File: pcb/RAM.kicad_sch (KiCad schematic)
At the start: 29 parts, among them U2 MT41K64M16TW-x

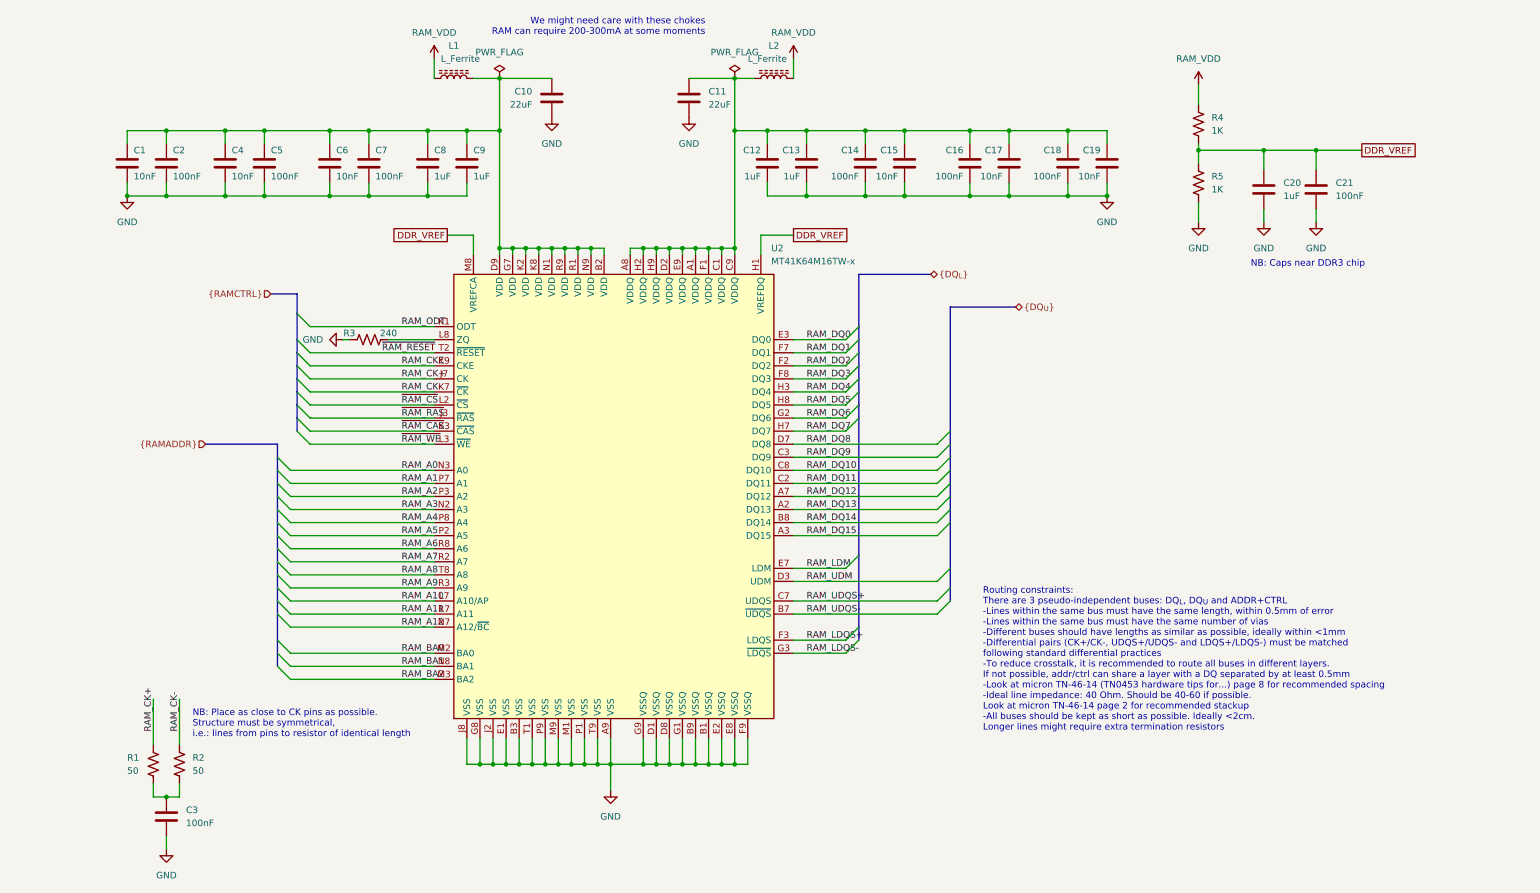
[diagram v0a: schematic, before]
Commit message: Initial footprint assignment
- Some edits to the schematic to improve readability
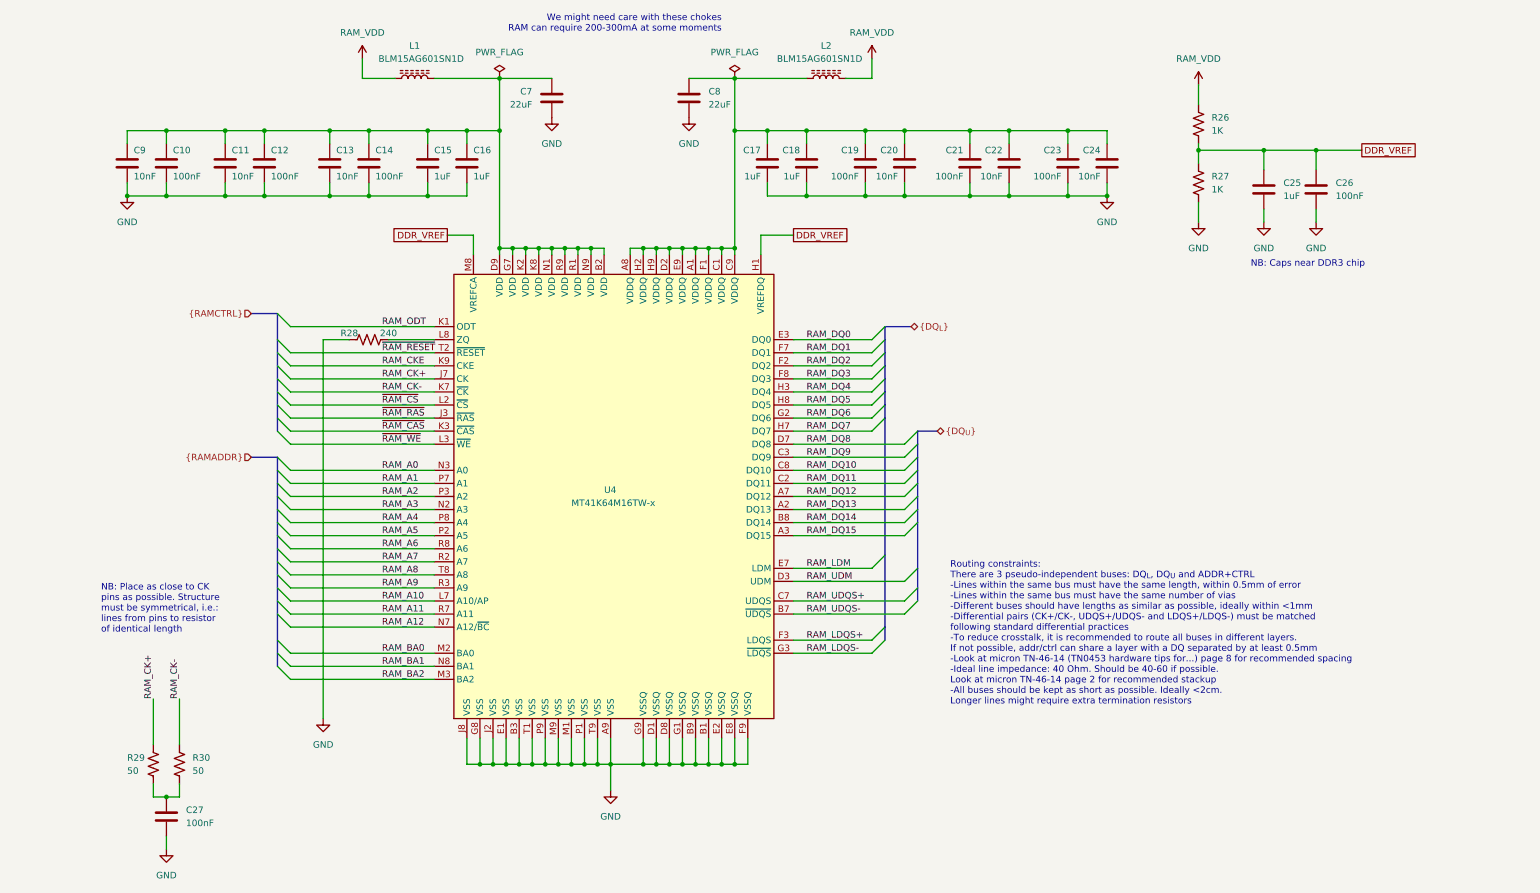
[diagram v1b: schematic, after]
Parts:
- C10: renamed from C2; footprint (none) -> Capacitor_SMD:C_0402_1005Metric
- C11: renamed from C4; footprint (none) -> Capacitor_SMD:C_0402_1005Metric
- C12: renamed from C5; footprint (none) -> Capacitor_SMD:C_0402_1005Metric
- C13: renamed from C6; footprint (none) -> Capacitor_SMD:C_0402_1005Metric
- C14: renamed from C7; footprint (none) -> Capacitor_SMD:C_0402_1005Metric
- C15: renamed from C8; footprint (none) -> Capacitor_SMD:C_0805_2012Metric
- C16: renamed from C9; footprint (none) -> Capacitor_SMD:C_0805_2012Metric
- C17: renamed from C12; footprint (none) -> Capacitor_SMD:C_0805_2012Metric
- C18: renamed from C13; footprint (none) -> Capacitor_SMD:C_0805_2012Metric
- C19: renamed from C14; footprint (none) -> Capacitor_SMD:C_0402_1005Metric
- C20: renamed from C15; footprint (none) -> Capacitor_SMD:C_0402_1005Metric
- C21: renamed from C16; footprint (none) -> Capacitor_SMD:C_0402_1005Metric
- C22: renamed from C17; footprint (none) -> Capacitor_SMD:C_0402_1005Metric
- C23: renamed from C18; footprint (none) -> Capacitor_SMD:C_0402_1005Metric
- C24: renamed from C19; footprint (none) -> Capacitor_SMD:C_0402_1005Metric
- C25: renamed from C20; footprint (none) -> Capacitor_SMD:C_0805_2012Metric
- C26: renamed from C21; footprint (none) -> Capacitor_SMD:C_0402_1005Metric
- C27: renamed from C3; footprint (none) -> Capacitor_SMD:C_0402_1005Metric
- C7: renamed from C10; footprint (none) -> Capacitor_SMD:C_1210_3225Metric
- C8: renamed from C11; footprint (none) -> Capacitor_SMD:C_1210_3225Metric
- C9: renamed from C1; footprint (none) -> Capacitor_SMD:C_0402_1005Metric
- L1, L2: value L_Ferrite -> BLM15AG601SN1D; footprint (none) -> Inductor_SMD:L_0402_1005Metric
- R26: renamed from R4; footprint (none) -> Resistor_SMD:R_0402_1005Metric
- R27: renamed from R5; footprint (none) -> Resistor_SMD:R_0402_1005Metric
- R28: renamed from R3; footprint (none) -> Resistor_SMD:R_0402_1005Metric
- R29: renamed from R1; footprint (none) -> Resistor_SMD:R_0402_1005Metric
- R30: renamed from R2; footprint (none) -> Resistor_SMD:R_0402_1005Metric
- U4: renamed from U2; footprint Package_BGA:BGA-96_9.0x13.0mm_Layout2x3x16_P0.8mm -> jonnew:MICRON_BGA96-10.5x8x1.3
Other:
- company: OEPS -> OEPS & Open Ephys, Inc.
- title: ECP5U85-BSE-USB Breakout board -> ECP5U85-BSE-USB Breakout Board
- moved on the sheet: L1, L2

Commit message: Rough PCB component placement
- This will change
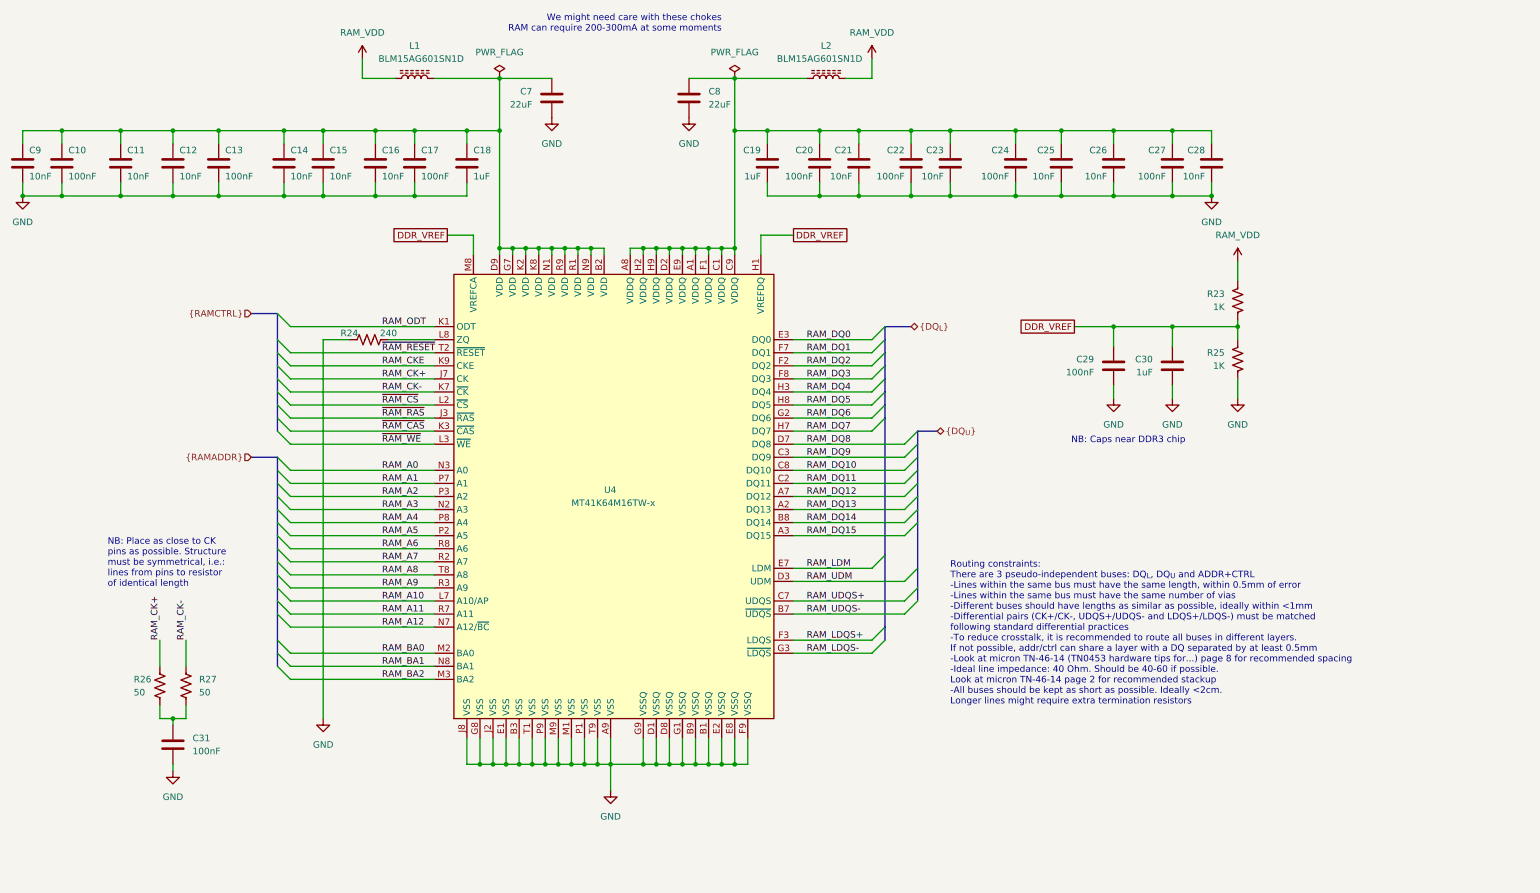
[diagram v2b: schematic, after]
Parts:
- removed C14: 100nF, Capacitor_SMD:C_0402_1005Metric, symbol Device:C
- removed C18: 1uF, Capacitor_SMD:C_0805_2012Metric, symbol Device:C
- added C12, C16, C25, C26, C28: 10nF, Capacitor_SMD:C_0402_1005Metric, symbol Device:C
- added C27: 100nF, Capacitor_SMD:C_0402_1005Metric, symbol Device:C
- C15: value 1uF -> 10nF; footprint Capacitor_SMD:C_0805_2012Metric -> Capacitor_SMD:C_0402_1005Metric
- C17: value 1uF -> 100nF; footprint Capacitor_SMD:C_0805_2012Metric -> Capacitor_SMD:C_0402_1005Metric
- C18: renamed from C16; footprint Capacitor_SMD:C_0805_2012Metric -> Capacitor_SMD:C_0603_1608Metric
- C19: value 100nF -> 1uF; footprint Capacitor_SMD:C_0402_1005Metric -> Capacitor_SMD:C_0603_1608Metric
- C20, C22, C24: value 10nF -> 100nF
- C21, C23: value 100nF -> 10nF
- C30: renamed from C25; footprint Capacitor_SMD:C_0805_2012Metric -> Capacitor_SMD:C_0603_1608Metric
- renumbered C12 to C13, C13 to C14, C26 to C29, C27 to C31, R26 to R23, R28 to R24, R27 to R25, R29 to R26, R30 to R27
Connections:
- net GND: now also C12.2, C16.2, C25.2, C26.2, C27.2, C28.2
- net at C10.1, C11.1, C13.1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: now also C17.1, C12.1, C16.1
- net at C19.1, C20.1, C21.1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: now also C25.1, C26.1, C27.1, C28.1; no longer C17.1
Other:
- moved on the sheet: C10, C11, C13, C14, C29, C30, C31, C9, R23, R25, R26, R27

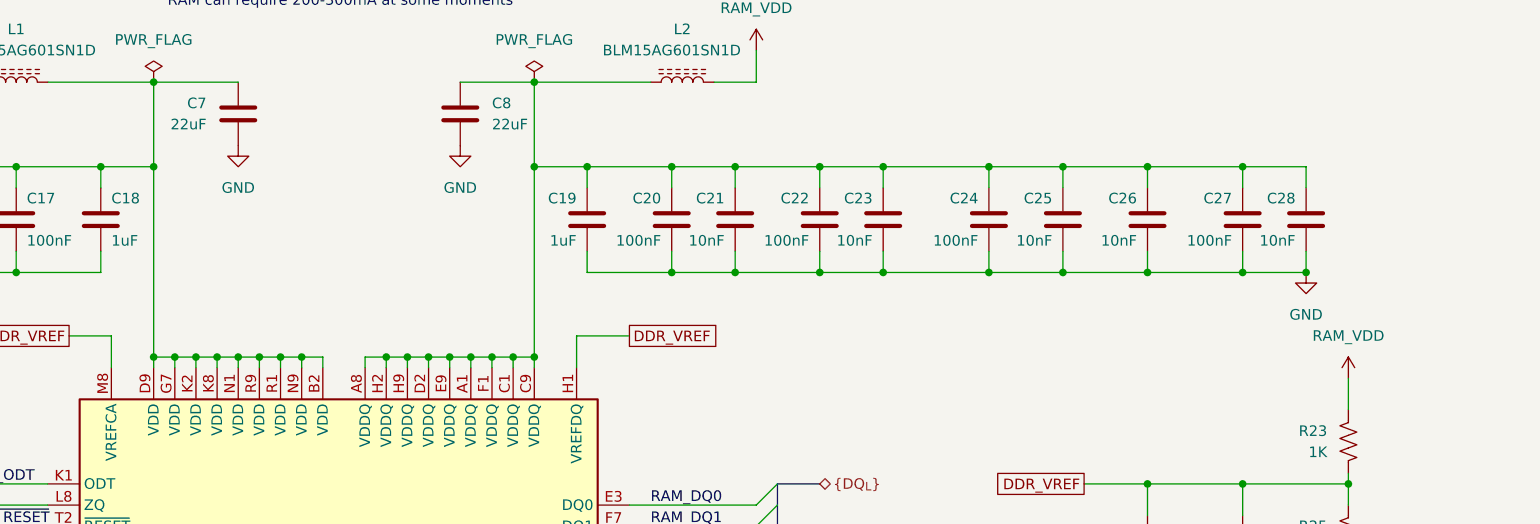
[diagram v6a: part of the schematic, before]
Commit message: Most of power routing
- Will need to retune the lengths again as final step, but only after
power is complete
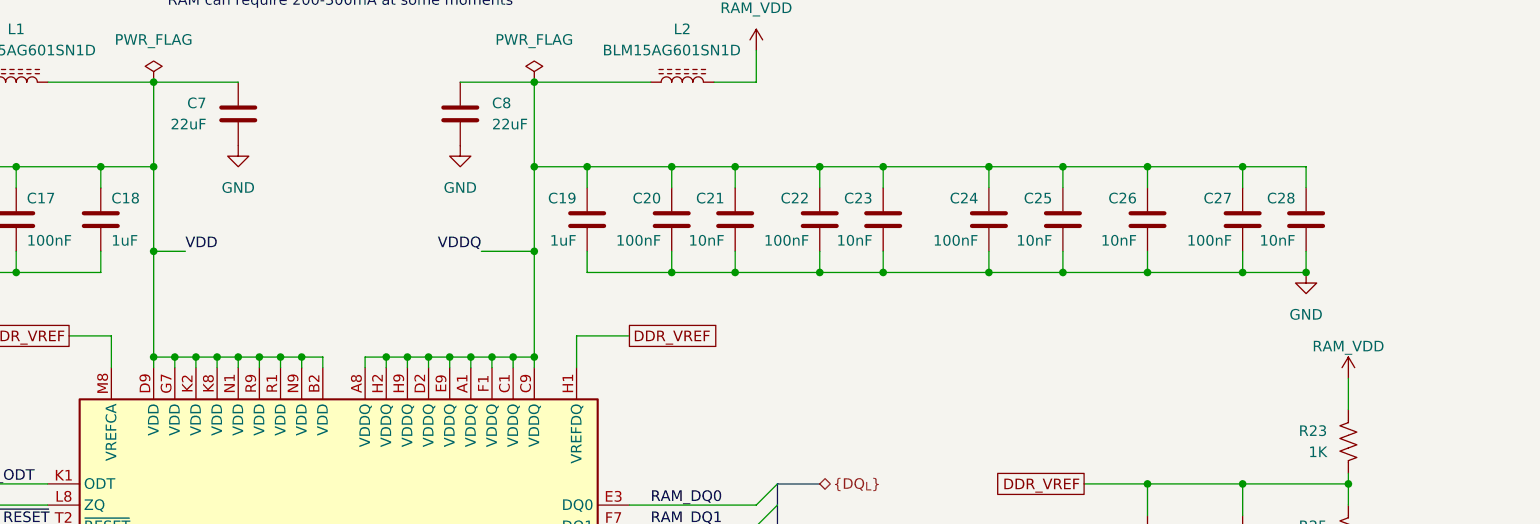
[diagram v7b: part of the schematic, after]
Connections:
- net VDD: now reaches C10.1, C11.1, C12.1, C13.1, C14.1, C15.1, C16.1, C17.1, C18.1, C7.1, C9.1, L1.2, U4.B2 (VDD), U4.D9 (VDD), U4.G7 (VDD), U4.K2 (VDD), U4.K8 (VDD), U4.N1 (VDD), U4.N9 (VDD), U4.R1 (VDD), U4.R9 (VDD)
- net VDDQ: now reaches C19.1, C20.1, C21.1, C22.1, C23.1, C24.1, C25.1, C26.1, C27.1, C28.1, C8.1, L2.1, U4.A1 (VDDQ), U4.A8 (VDDQ), U4.C1 (VDDQ), U4.C9 (VDDQ), U4.D2 (VDDQ), U4.E9 (VDDQ), U4.F1 (VDDQ), U4.H2 (VDDQ), U4.H9 (VDDQ)
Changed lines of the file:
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@@
   (junction (at 6.35 50.8) (diameter 0) (color 0 0 0 0)
   )
+  (junction (at 99.06 48.26) (diameter 0) (color 0 0 0 0)
+  )
   (junction (at 237.49 50.8) (diameter 0) (color 0 0 0 0)
   )
@@
   (junction (at 44.45 38.1) (diameter 0) (color 0 0 0 0)
   )
+  (junction (at 144.78 48.26) (diameter 0) (color 0 0 0 0)
+  )
   (junction (at 99.06 38.1) (diameter 0) (color 0 0 0 0)
   )
@@
     (stroke (width 0) (type default) (color 0 0 0 0))
   )
+  (wire (pts (xy 138.43 48.26) (xy 144.78 48.26))
+    (stroke (width 0) (type default) (color 0 0 0 0))
+  )
   (wire (pts (xy 237.49 40.64) (xy 237.49 38.1))
     (stroke (width 0) (type default) (color 0 0 0 0))
@@
     (stroke (width 0) (type default) (color 0 0 0 0))
   )
+  (wire (pts (xy 99.06 48.26) (xy 102.87 48.26))
+    (stroke (width 0) (type default) (color 0 0 0 0))
+  )
   (wire (pts (xy 144.78 156.21) (xy 144.78 161.29))
     (stroke (width 0) (type default) (color 0 0 0 0))
@@
     (stroke (width 0) (type default) (color 0 0 0 0))
   )
+  (wire (pts (xy 99.06 48.26) (xy 99.06 60.96))
+    (stroke (width 0) (type default) (color 0 0 0 0))
+  )
   (wire (pts (xy 58.42 86.36) (xy 86.36 86.36))
     (stroke (width 0) (type default) (color 0 0 0 0))
@@
     (stroke (width 0) (type default) (color 0 0 0 0))
   )
-  (wire (pts (xy 99.06 38.1) (xy 99.06 60.96))
+  (wire (pts (xy 99.06 38.1) (xy 99.06 48.26))
     (stroke (width 0) (type default) (color 0 0 0 0))
   )
@@
     (stroke (width 0) (type default) (color 0 0 0 0))
   )
+  (wire (pts (xy 144.78 48.26) (xy 144.78 60.96))
+    (stroke (width 0) (type default) (color 0 0 0 0))
+  )
   (bus (pts (xy 173.99 134.62) (xy 173.99 120.65))
     (stroke (width 0) (type default) (color 0 0 0 0))
@@
     (stroke (width 0) (type default) (color 0 0 0 0))
   )
-  (wire (pts (xy 144.78 38.1) (xy 144.78 60.96))
+  (wire (pts (xy 144.78 38.1) (xy 144.78 48.26))
     (stroke (width 0) (type default) (color 0 0 0 0))
   )
@@
     (effects (font (size 1.27 1.27)) (justify left bottom))
   )
+  (label "VDDQ" (at 138.43 48.26 180)
+    (effects (font (size 1.27 1.27)) (justify right bottom))
+  )
   (label "~{RAM_WE}" (at 76.2 99.06 0)
     (effects (font (size 1.27 1.27)) (justify left bottom))
@@
   )
   (label "RAM_CK+" (at 76.2 86.36 0)
+    (effects (font (size 1.27 1.27)) (justify left bottom))
+  )
+  (label "VDD" (at 102.87 48.26 0)
     (effects (font (size 1.27 1.27)) (justify left bottom))
   )
@@
   )
   (symbol (lib_id "ecp5u85-bse-usb:RAM_VDD") (at 242.57 63.5 0) (mirror y) (unit 1)
-    (in_bom yes) (on_board yes) (fields_autoplaced)
+    (in_bom yes) (on_board yes)
     (property "Reference" "#PWR042" (id 0) (at 242.57 67.31 0)
       (effects (font (size 1.27 1.27)) hide)
     )
-    (property "Value" "RAM_VDD" (id 1) (at 242.57 58.42 0))
+    (property "Value" "RAM_VDD" (id 1) (at 242.57 59.69 0))
     (property "Footprint" "" (id 2) (at 242.57 63.5 0)
       (effects (font (size 1.27 1.27)) hide)

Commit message: Rev. A before fab comments
- Added gerbers, mount positions, etc.
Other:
- moved on the sheet: C10, C11, C12, C13, C14, C15, C16, C17, C18, C19, C20, C21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
